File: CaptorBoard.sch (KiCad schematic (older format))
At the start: 54 parts, among them CON1 MINI-USB-SHELD-MC32598, P1 Prog, P2 POWER, Q1 IRLM6402TRPBF, SW1 SW_PUSH, U1 PIC32MX795F512H-80I-PT, U2 MRF24J40MA-I-RM, U3 HTU21, U4 MPL115A2, U5 VTX-214-003-105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

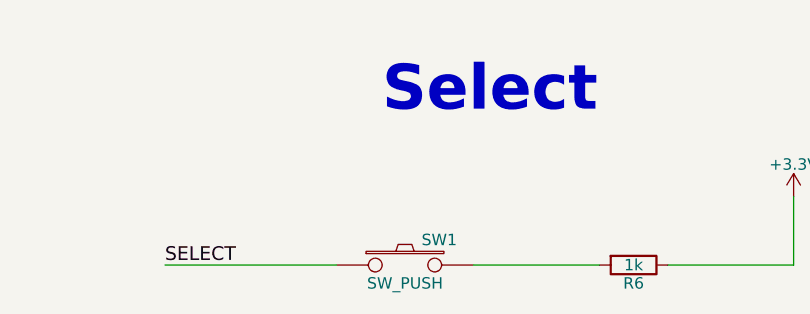
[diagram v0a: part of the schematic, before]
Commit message: Set all foot print
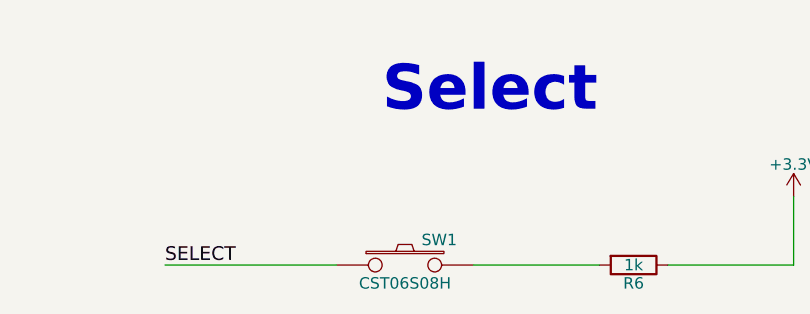
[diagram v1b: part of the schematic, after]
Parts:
- C1, C10, C11, C12, C13, C14, C15, C3, C4, C6, C7, C8, C9: footprint (none) -> Capacitors_SMD:C_0805
- C16: footprint (none) -> Capacitors_SMD:c_elec_4x5.3
- C2: footprint (none) -> Capacitors_SMD:c_elec_5x5.3
- C5: footprint (none) -> SMD_Packages:SMD-1206_Pol
- D1, D2: footprint (none) -> Diodes_SMD:Diode-MiniMELF_Standard
- D10, D9: footprint (none) -> Diodes_ThroughHole:Diode_DO-41_SOD81_Horizontal_RM10
- D3, D4, D5, D6, D7: footprint (none) -> LEDs:LED-1206
- D8: footprint (none) -> Diodes_SMD:Diode-SMB_Standard
- F1: footprint (none) -> Fuse_Holders_and_Fuses:Fuseholder5x20_horiz_SemiClosed_Casing10x25mm
- P1: footprint (none) -> Pin_Headers:Pin_Header_Straight_1x06
- P2: footprint (none) -> Connect:bornier4
- R1, R10, R11, R12, R13, R2, R3, R4, R5, R6, R7, R8, R9: footprint (none) -> Resistors_SMD:R_0805
- SW1: value SW_PUSH -> CST06S08H; footprint (none) -> pfo:CST06S
- U2: footprint MODULE -> pfo:MRF24J40MA
- U4: footprint MODULE -> pfo:MPL115A2
- U5: footprint Housings_DFN_QFN:DFN-6-1EP_3x3mm_Pitch0.95mm -> pfo:VTX-214-003-105

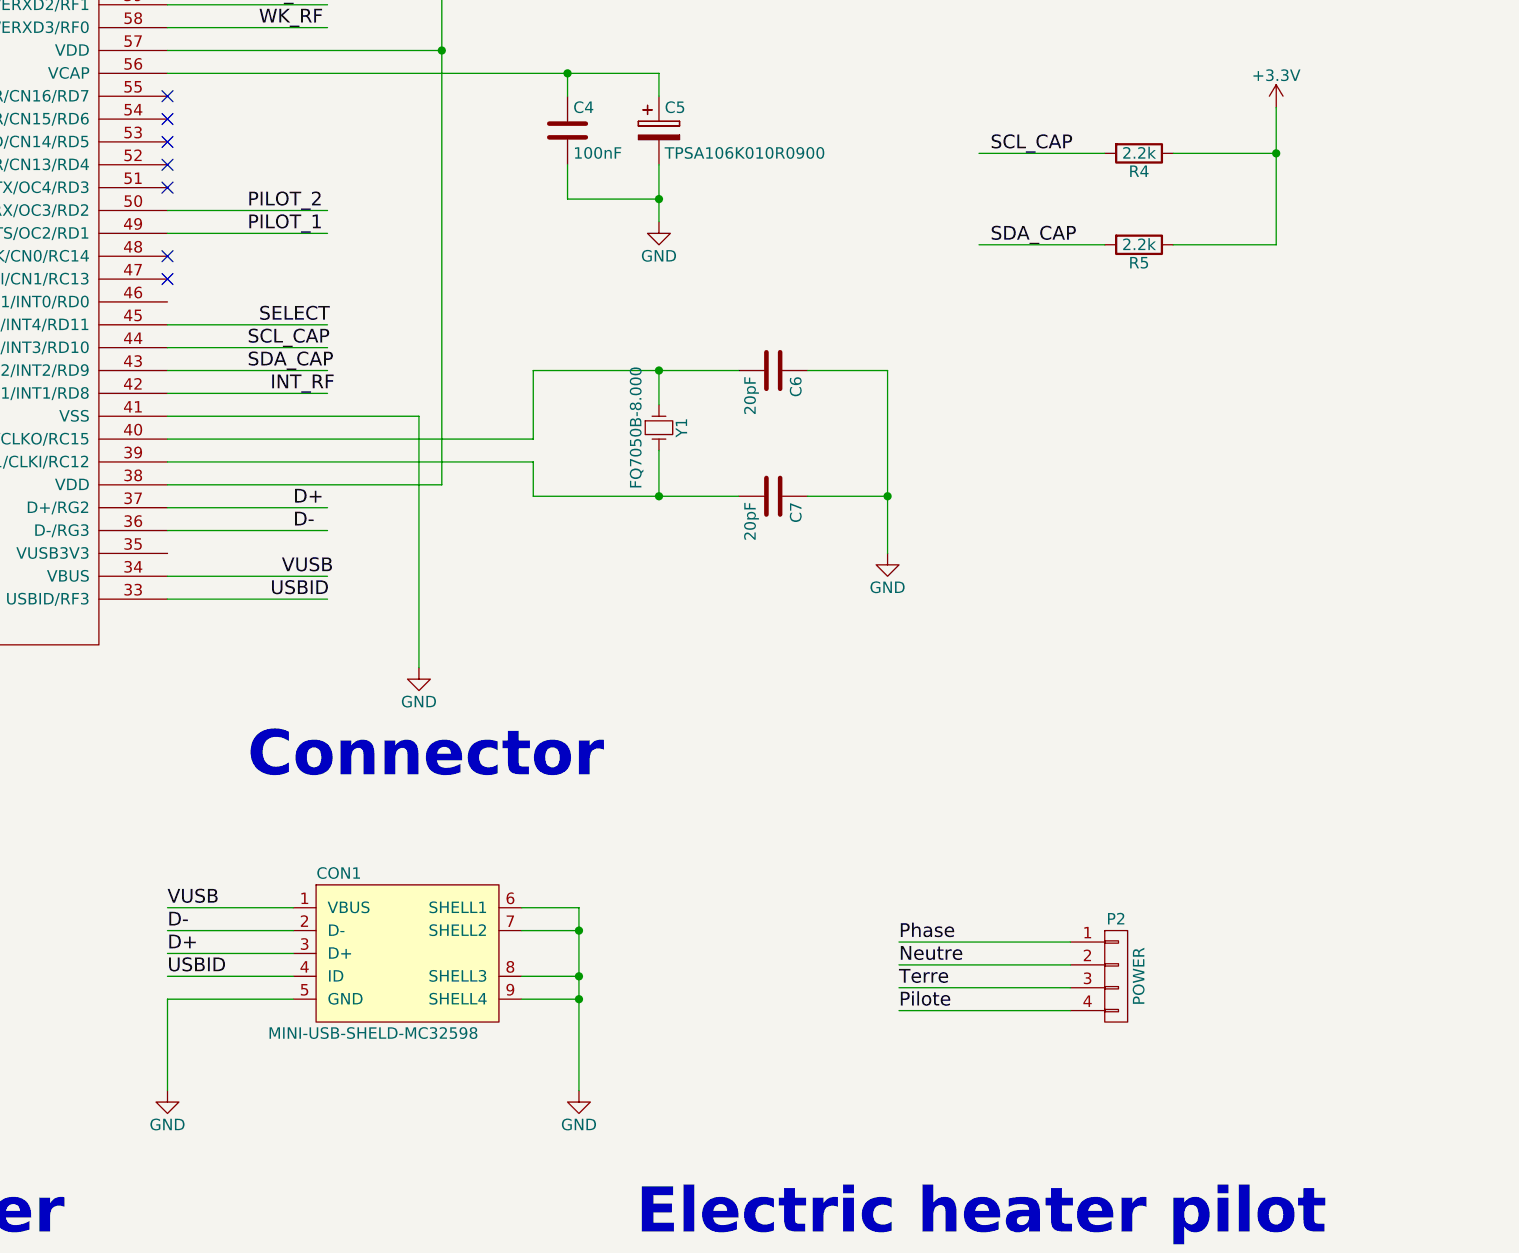
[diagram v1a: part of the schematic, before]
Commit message: Change LED foot print Add extension conector
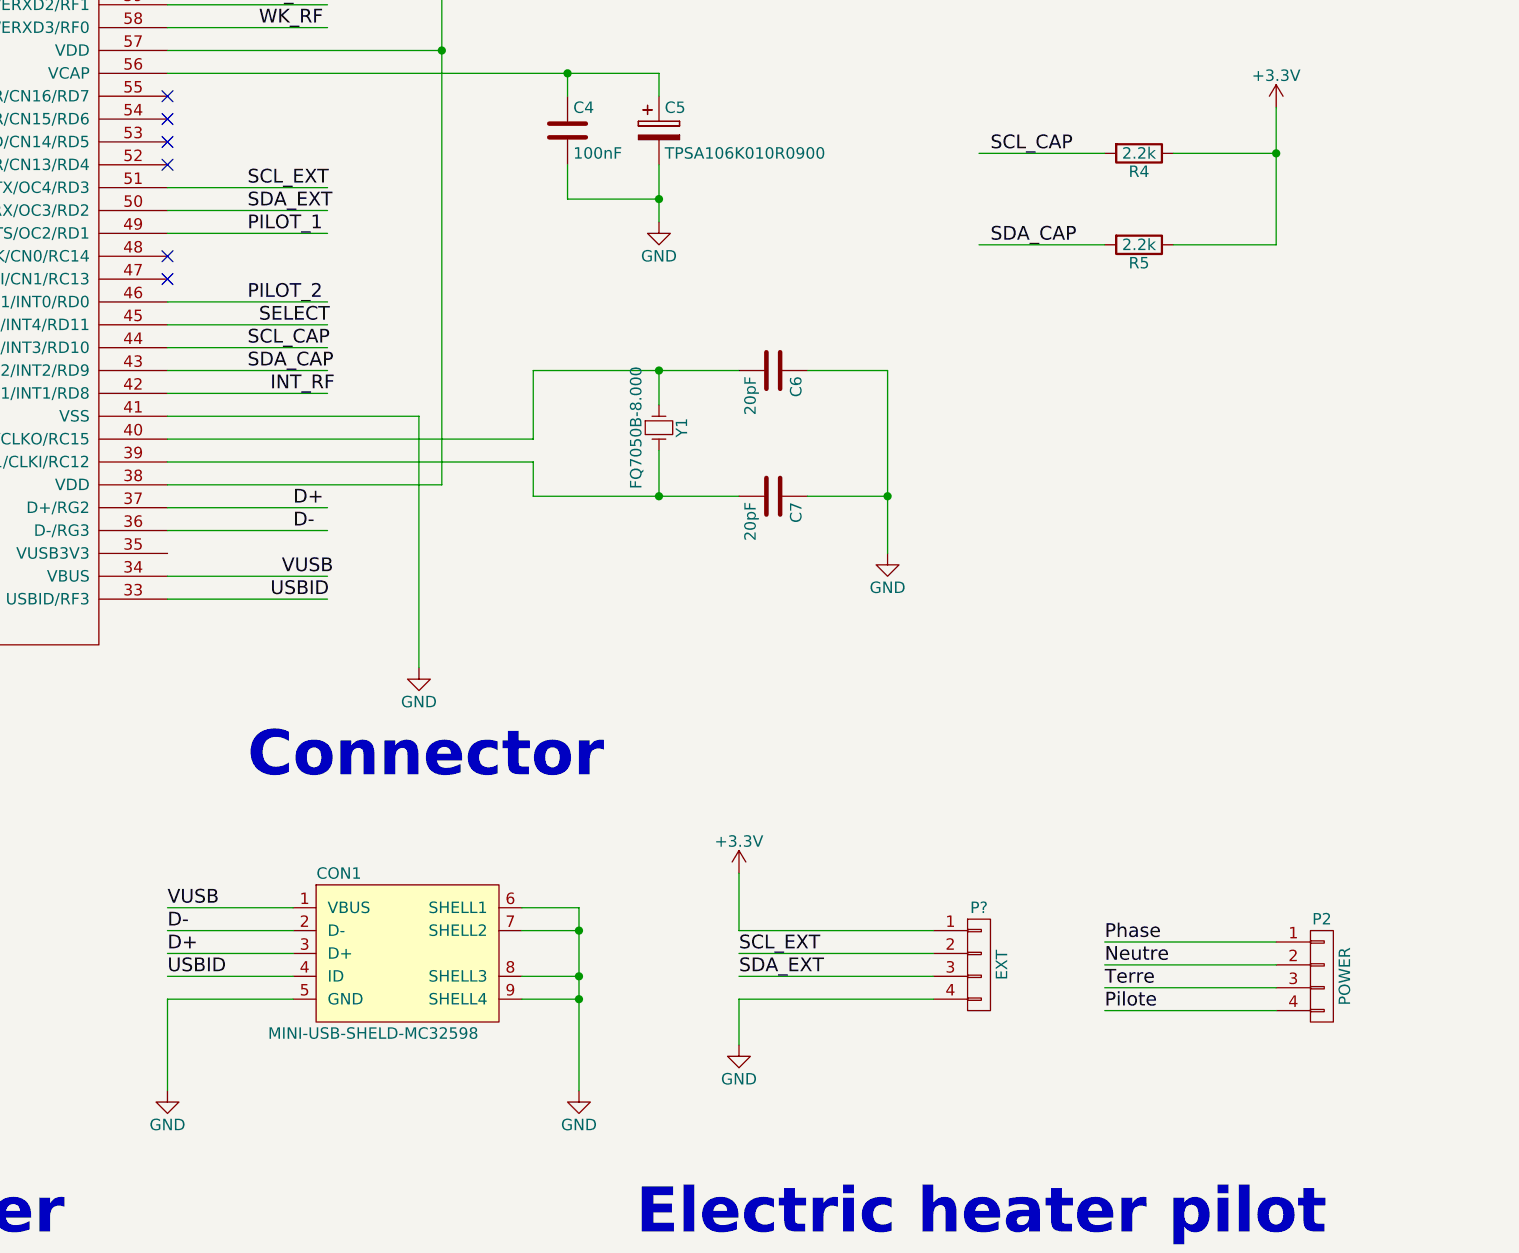
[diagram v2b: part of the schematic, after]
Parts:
- added P?: EXT, symbol CONN_01X04
- CON1: footprint Connect:USB_Mini-B -> pfo:USB_Mini-B
- D3, D4, D5, D6, D7: footprint LEDs:LED-1206 -> pfo:LED-1206-Guide
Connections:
- net labels added: SCL_EXT, SDA_EXT
- wire segments 209 -> 217
- no-connect marks 24 -> 23
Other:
- moved on the sheet: P2
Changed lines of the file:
@@
 Text Label 11000 2050 0    60   ~ 0
 WK_RF
-Text Label 10950 2850 0    60   ~ 0
+Text Label 10950 3250 0    60   ~ 0
 PILOT_2
 Text Label 10950 2950 0    60   ~ 0
@@
 F 0 "CON1" H 11350 6450 50  0000 C CNN
 F 1 "MINI-USB-SHELD-MC32598" H 11500 5750 50  0000 C CNN
-F 2 "Connect:USB_Mini-B" H 11650 6000 50  0001 C CNN
+F 2 "pfo:USB_Mini-B" H 11650 6000 50  0001 C CNN
 F 3 "" H 11650 6000 50  0000 C CNN
 	1    11650 6100
@@
 NoConn ~ 10600 2550
 NoConn ~ 10600 2650
-NoConn ~ 10600 2750
 NoConn ~ 10600 3050
 NoConn ~ 10600 3150
@@
 F 0 "D3" H 6100 8250 50  0000 C CNN
 F 1 "POWER" H 6100 8050 50  0000 C CNN
-F 2 "LEDs:LED-1206" H 6100 8150 60  0001 C CNN
+F 2 "pfo:LED-1206-Guide" H 6100 8150 60  0001 C CNN
 F 3 "" H 6100 8150 60  0000 C CNN
 	1    6100 8150
@@
 F 0 "D4" H 6100 8600 50  0000 C CNN
 F 1 "CONF" H 6100 8400 50  0000 C CNN
-F 2 "LEDs:LED-1206" H 6100 8500 60  0001 C CNN
+F 2 "pfo:LED-1206-Guide" H 6100 8500 60  0001 C CNN
 F 3 "" H 6100 8500 60  0000 C CNN
 	1    6100 8500
@@
 F 0 "D5" H 6100 8950 50  0000 C CNN
 F 1 "ECO" H 6100 8750 50  0000 C CNN
-F 2 "LEDs:LED-1206" H 6100 8850 60  0001 C CNN
+F 2 "pfo:LED-1206-Guide" H 6100 8850 60  0001 C CNN
 F 3 "" H 6100 8850 60  0000 C CNN
 	1    6100 8850
@@
 F 0 "D6" H 6100 9300 50  0000 C CNN
 F 1 "CONF-1°C" H 6100 9100 50  0000 C CNN
-F 2 "LEDs:LED-1206" H 6100 9200 60  0001 C CNN
+F 2 "pfo:LED-1206-Guide" H 6100 9200 60  0001 C CNN
 F 3 "" H 6100 9200 60  0000 C CNN
 	1    6100 9200
@@
 F 0 "D7" H 6100 9650 50  0000 C CNN
 F 1 "CONF-2°C" H 6100 9450 50  0000 C CNN
-F 2 "LEDs:LED-1206" H 6100 9550 60  0001 C CNN
+F 2 "pfo:LED-1206-Guide" H 6100 9550 60  0001 C CNN
 F 3 "" H 6100 9550 60  0000 C CNN
 	1    6100 9550
@@
 L CONN_01X04 P2
 U 1 1 5525D421
-P 14750 6200
-F 0 "P2" H 14750 6450 50  0000 C CNN
-F 1 "POWER" V 14850 6200 50  0000 C CNN
-F 2 "Connect:bornier4" H 14750 6200 60  0001 C CNN
-F 3 "" H 14750 6200 60  0000 C CNN
-	1    14750 6200
-	1    0    0    -1
-$EndComp
-Text Label 13800 6050 0    60   ~ 0
+P 15650 6200
+F 0 "P2" H 15650 6450 50  0000 C CNN
+F 1 "POWER" V 15750 6200 50  0000 C CNN
+F 2 "Connect:bornier4" H 15650 6200 60  0001 C CNN
+F 3 "" H 15650 6200 60  0000 C CNN
+	1    15650 6200
+	1    0    0    -1
+$EndComp
+Text Label 14700 6050 0    60   ~ 0
 Phase
-Text Label 13800 6150 0    60   ~ 0
+Text Label 14700 6150 0    60   ~ 0
 Neutre
-Text Label 13800 6250 0    60   ~ 0
+Text Label 14700 6250 0    60   ~ 0
 Terre
-Text Label 13800 6350 0    60   ~ 0
+Text Label 14700 6350 0    60   ~ 0
 Pilote
 Text Notes 10950 5350 0    197  ~ 39
@@
 	10600 2050 11300 2050
 Wire Wire Line
-	10600 2850 11300 2850
+	10600 3250 11300 3250
 Wire Wire Line
 	10600 2950 11300 2950
@@
 	5500 10900 4750 10900
 Wire Wire Line
-	14550 6050 13800 6050
-Wire Wire Line
-	14550 6150 13800 6150
-Wire Wire Line
-	14550 6250 13800 6250
-Wire Wire Line
-	14550 6350 13800 6350
+	15450 6050 14700 6050
+Wire Wire Line
+	15450 6150 14700 6150
+Wire Wire Line
+	15450 6250 14700 6250
+Wire Wire Line
+	15450 6350 14700 6350
 Wire Wire Line
 	11500 8050 11700 8050
@@
 Text Label 15350 8750 0    60   ~ 0
 Pilote
+$Comp
+L CONN_01X04 P?
+U 1 1 5533F0E1
+P 14150 6150
+F 0 "P?" H 14150 6400 50  0000 C CNN
+F 1 "EXT" V 14250 6150 50  0000 C CNN
+F 2 "" H 14150 6150 60  0000 C CNN
+F 3 "" H 14150 6150 60  0000 C CNN
+	1    14150 6150
+	1    0    0    -1
+$EndComp
+Wire Wire Line
+	13950 6000 13100 6000
+Wire Wire Line
+	13950 6100 13100 6100
+Wire Wire Line
+	13950 6200 13100 6200
+Wire Wire Line
+	13950 6300 13100 6300
+$Comp
+L GND #PWR?
+U 1 1 5533FC25
+P 13100 6500
+F 0 "#PWR?" H 13100 6250 50  0001 C CNN
+F 1 "GND" H 13100 6350 50  0000 C CNN
+F 2 "" H 13100 6500 60  0000 C CNN
+F 3 "" H 13100 6500 60  0000 C CNN
+	1    13100 6500
+	1    0    0    -1
+$EndComp
+$Comp
+L +3.3V #PWR?
+U 1 1 5533FE1F
+P 13100 5750
+F 0 "#PWR?" H 13100 5600 50  0001 C CNN
+F 1 "+3.3V" H 13100 5890 50  0000 C CNN
+F 2 "" H 13100 5750 60  0000 C CNN
+F 3 "" H 13100 5750 60  0000 C CNN
+	1    13100 5750
+	1    0    0    -1
+$EndComp
+Wire Wire Line
+	13100 6000 13100 5750
+Wire Wire Line
+	13100 6300 13100 6500
+Wire Wire Line
+	10600 2850 11300 2850
+Wire Wire Line
+	10600 2750 11300 2750
+Text Label 10950 2850 0    60   ~ 0
+SDA_EXT
+Text Label 10950 2750 0    60   ~ 0
+SCL_EXT
+Text Label 13100 6100 0    60   ~ 0
+SCL_EXT
+Text Label 13100 6200 0    60   ~ 0
+SDA_EXT
 $EndSCHEMATC
